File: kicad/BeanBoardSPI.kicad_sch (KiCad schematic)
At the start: 40 parts, among them J1 Conn_01x03_Pin, J10 SPI6, J11 GPO, J12 Conn_01x10_Pin, J13 Conn_01x10_Pin, J14 GPI, J15 Power, J2 Conn_01x16_Pin, J3 Conn_01x16_Pin, J4 SPI0 (RA8875), J5 SPI1, J6 SPI2, J7 SPI3, J8 SPI4, J9 SPI5, U1 74HC244, U10 74HC138, U11 74HC165, U12 74HC244, U13 74HC02, U2 74HC164, U3 74HC165, U4 74HC373, U5 74HC165, U6 74HC165, U8 74HC02, U9 74HC74

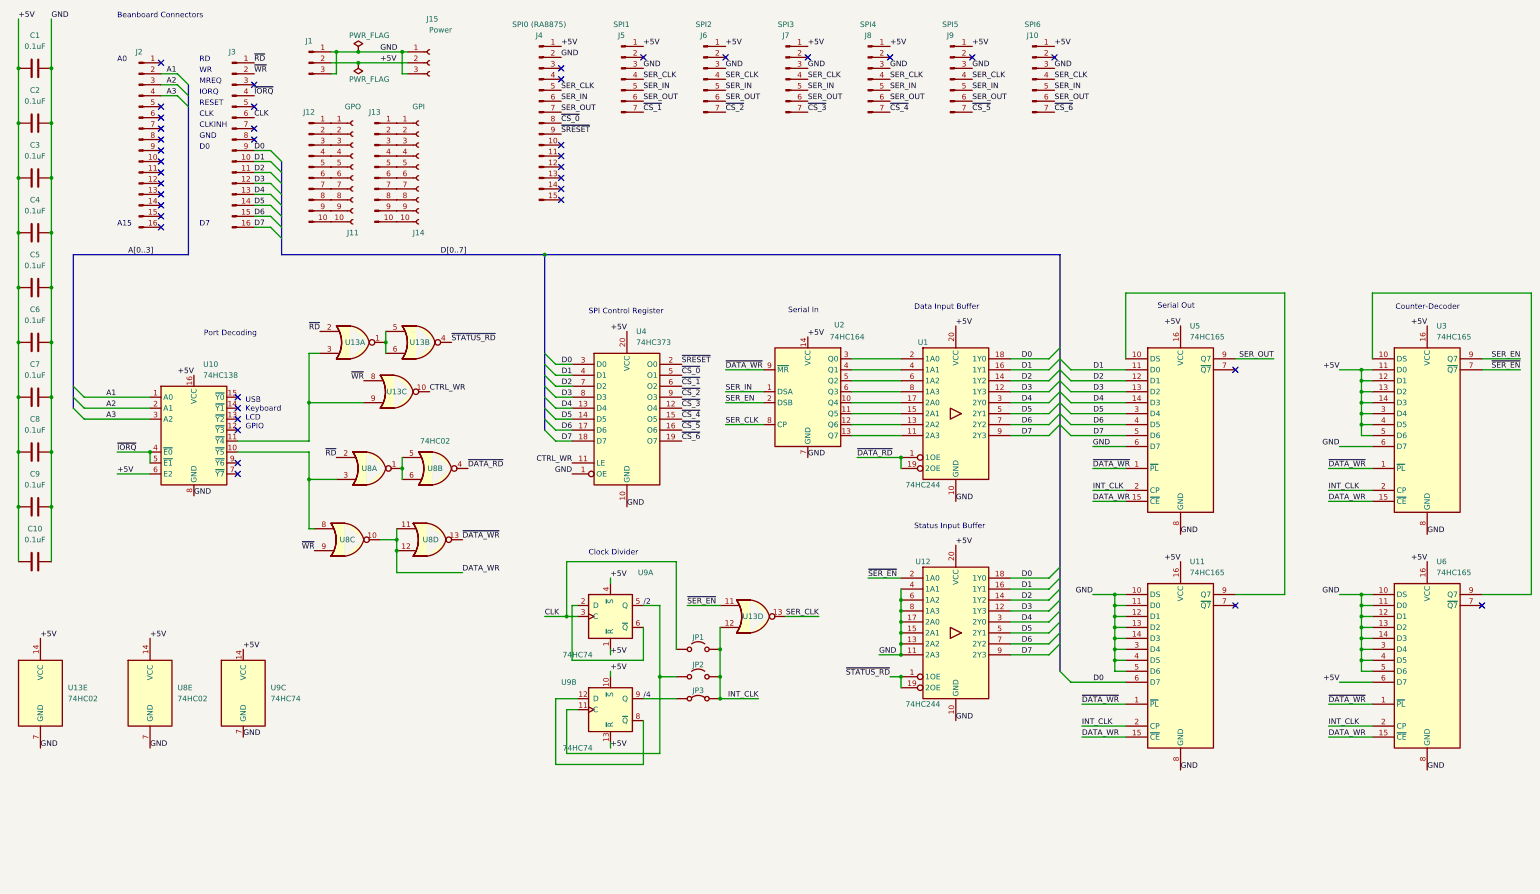
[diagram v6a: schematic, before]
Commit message: schematic
renumber components
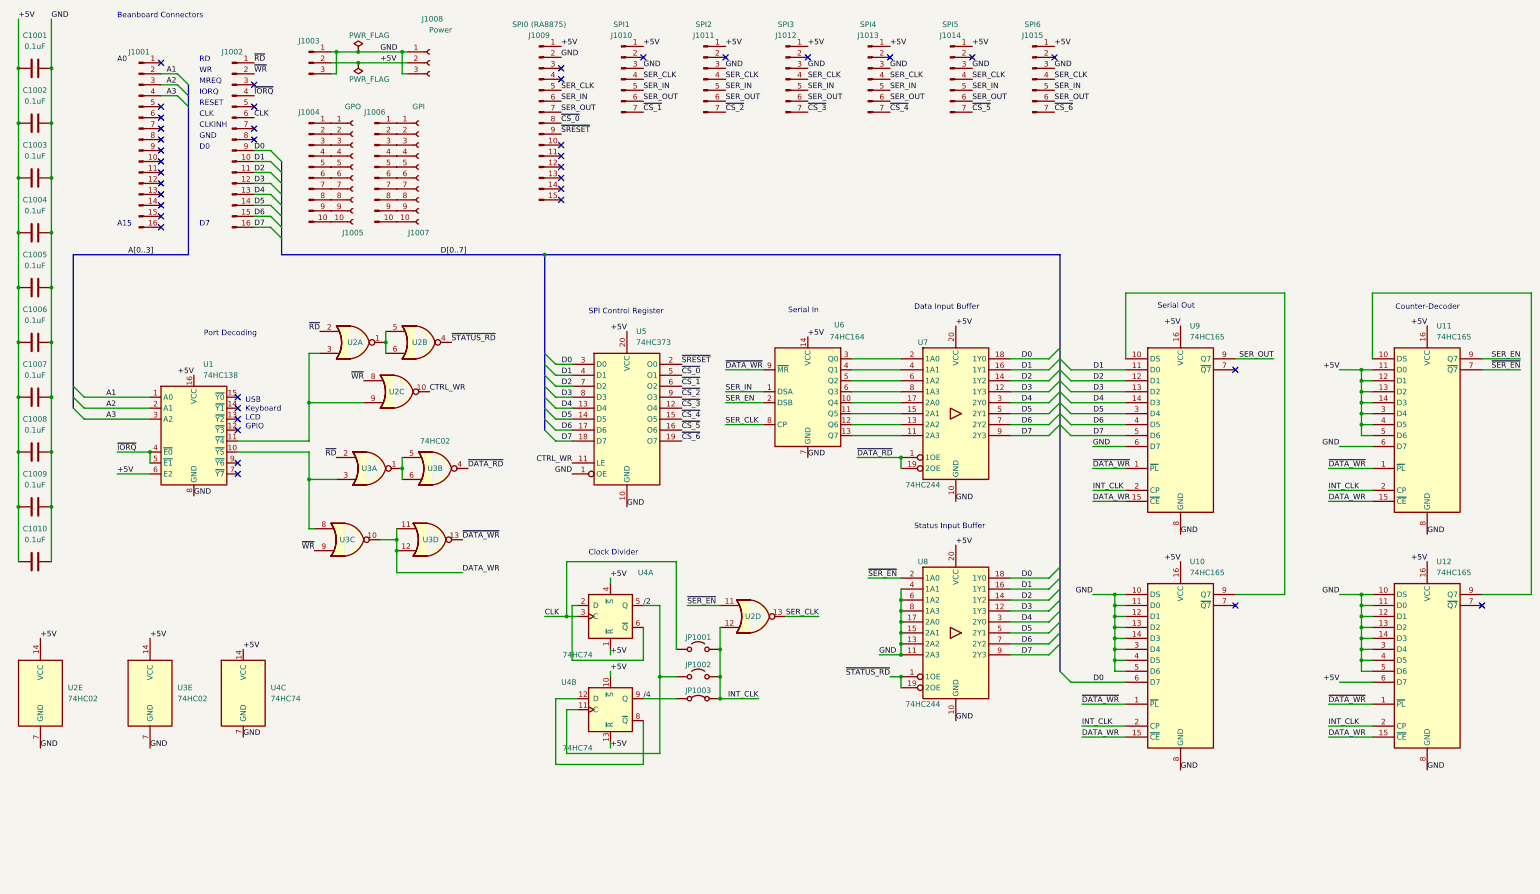
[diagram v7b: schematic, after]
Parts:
- renumbered C1 to C1001, C2 to C1002, C3 to C1003, C4 to C1004, C5 to C1005, C6 to C1006, C7 to C1007, C8 to C1008, C9 to C1009, C10 to C1010, J2 to J1001, J3 to J1002, J1 to J1003, J12 to J1004, J11 to J1005, J13 to J1006, J14 to J1007, J15 to J1008, J4 to J1009, J5 to J1010, J6 to J1011, J7 to J1012, J8 to J1013, J9 to J1014, J10 to J1015, JP1 to JP1001, JP2 to JP1002, JP3 to JP1003, U10 to U1, U11 to U10, U3 to U11, U6 to U12, U13 to U2, U8 to U3, U9 to U4, U4 to U5, U2 to U6, U1 to U7, U12 to U8, U5 to U9

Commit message: layout
footprints
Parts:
- U10, U11, U12, U9: footprint Package_DIP:DIP-16_W7.62mm -> Package_DIP:DIP-16_W7.62mm_Socket
- U7, U8: footprint Package_DIP:DIP-20_W7.62mm -> Package_DIP:DIP-20_W7.62mm_Socket
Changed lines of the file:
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@@
 			)
 		)
-		(property "Footprint" "Package_DIP:DIP-16_W7.62mm"
+		(property "Footprint" "Package_DIP:DIP-16_W7.62mm_Socket"
 			(at 275.59 97.79 0)
 			(hide yes)
@@
 			)
 		)
-		(property "Footprint" "Package_DIP:DIP-20_W7.62mm"
+		(property "Footprint" "Package_DIP:DIP-20_W7.62mm_Socket"
 			(at 223.52 95.25 0)
 			(hide yes)
@@
 			)
 		)
-		(property "Footprint" "Package_DIP:DIP-16_W7.62mm"
+		(property "Footprint" "Package_DIP:DIP-16_W7.62mm_Socket"
 			(at 332.74 152.4 0)
 			(hide yes)
@@
 			)
 		)
-		(property "Footprint" "Package_DIP:DIP-16_W7.62mm"
+		(property "Footprint" "Package_DIP:DIP-16_W7.62mm_Socket"
 			(at 332.74 97.79 0)
 			(hide yes)
@@
 			)
 		)
-		(property "Footprint" "Package_DIP:DIP-20_W7.62mm"
+		(property "Footprint" "Package_DIP:DIP-20_W7.62mm_Socket"
 			(at 223.52 146.05 0)
 			(hide yes)
@@
 			)
 		)
-		(property "Footprint" "Package_DIP:DIP-16_W7.62mm"
+		(property "Footprint" "Package_DIP:DIP-16_W7.62mm_Socket"
 			(at 275.59 152.4 0)
 			(hide yes)
